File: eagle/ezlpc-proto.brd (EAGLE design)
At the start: 38.1 x 22.9 mm, 61 parts, among them J1 MICRO USB, Q1 12Mhz, T1 MMBT3906, U1 PRTR5V0U2X, U2 MIC5225-3.3v, U3 LPC11U35FHI33/501

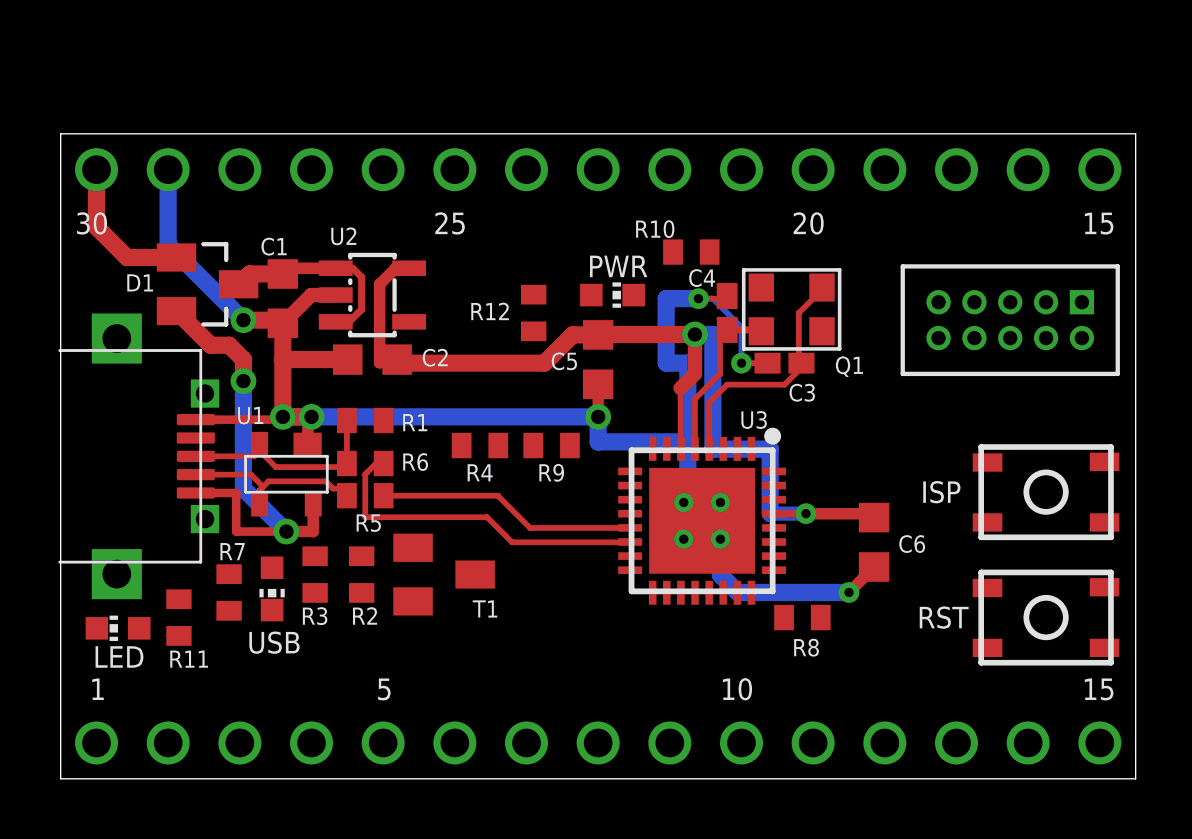
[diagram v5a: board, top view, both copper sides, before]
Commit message: More layout cleanup.
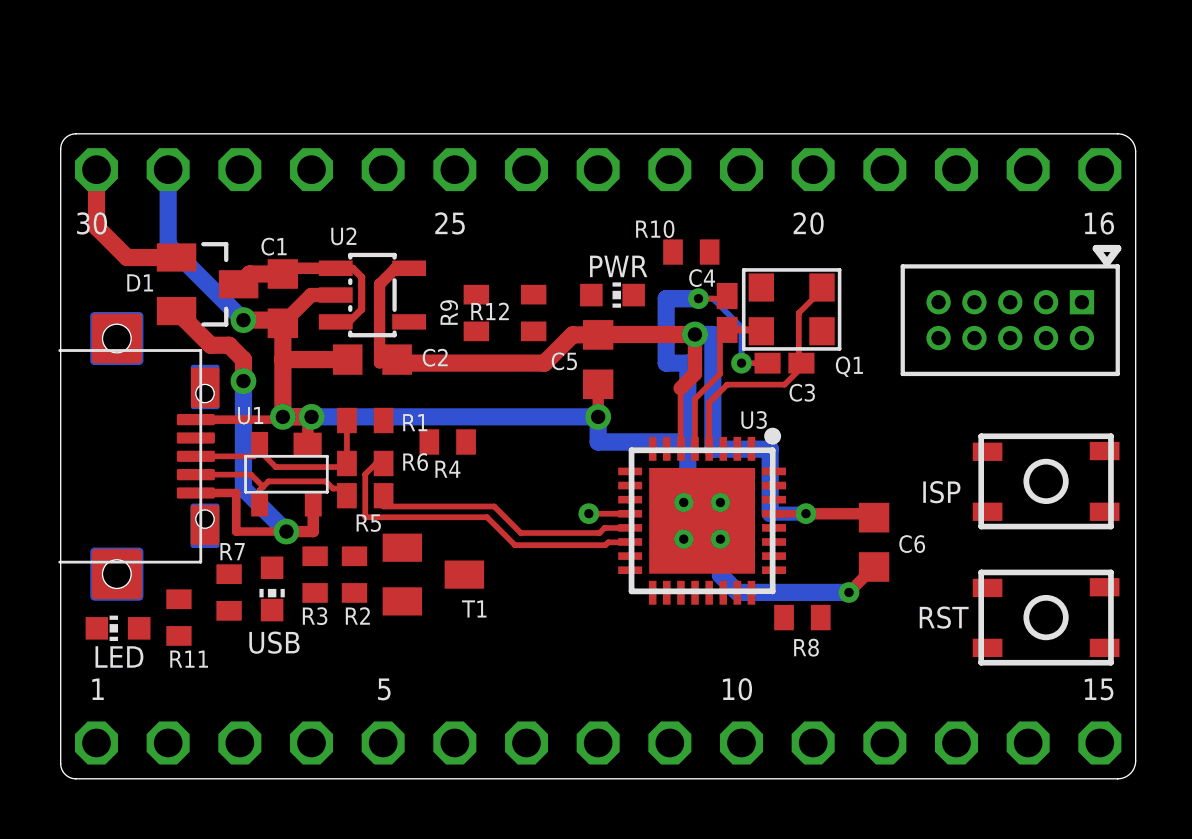
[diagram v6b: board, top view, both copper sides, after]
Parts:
- moved R9 5.40 mm to (14.7, 16.5), turned to 90 degrees
- moved R4 1.15 mm to (13.7, 11.9)
- moved S2 0.38 mm to (34.9, 10.5)
- moved T1 0.38 mm to (13.2, 7.24)
- moved R2 0.25 mm to (10.4, 7.24)
- renumbered JP1 to J2, JP10 to TP3, JP11 to TP5, JP12 to TP25, JP13 to TP7, JP14 to TP8, JP15 to TP9, JP16 to TP10, JP17 to TP11, JP18 to TP12, JP19 to TP15, JP2 to TP20, JP20 to TP16, JP21 to TP18, JP22 to TP21, JP23 to TP2, JP24 to TP6, JP25 to TP13, JP26 to TP14, JP27 to TP19, JP28 to TP24, JP29 to TP27, JP3 to TP17, JP30 to TP29, JP31 to TP30, JP4 to TP22, JP5 to TP26, JP6 to TP23, JP7 to TP28, JP8 to TP4, JP9 to TP1
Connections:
- new net PIO0_9-SWD6: J2.6
- net PIO0_6-CONNECT: now also TP3.1; no longer TP4.1
- net PIO0_8: now also TP4.1; no longer TP3.1
- net PIO0_9: no longer J2.6
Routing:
- net PIO0_21: track 0.00 -> 1.46 mm, vias 0 -> 1
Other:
- outline, holes or cut-outs redrawn
- board text added: "16"
